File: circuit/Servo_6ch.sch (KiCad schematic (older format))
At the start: 24 parts, among them IC1 TLP521, IC2 TLP521, IC3 TLP521, IC4 TLP521, IC5 TLP521, IC6 TLP521, J3 servo0, J4 servo1, J5 servo2, J6 servo0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

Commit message: 回路図と部品表完了
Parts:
- J3, J4, J5, J6, J7, J8: footprint (none) -> YASU:XA_3Pin
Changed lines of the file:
@@
 F 0 "J3" H 5400 2650 50  0000 C CNN
 F 1 "servo0" V 5500 2450 50  0000 C CNN
-F 2 "" H 5400 2450 50  0001 C CNN
+F 2 "YASU:XA_3Pin" H 5400 2450 50  0001 C CNN
 F 3 "" H 5400 2450 50  0001 C CNN
 	1    5400 2450
@@
 F 0 "J5" H 5400 5050 50  0000 C CNN
 F 1 "servo2" V 5500 4850 50  0000 C CNN
-F 2 "" H 5400 4850 50  0001 C CNN
+F 2 "YASU:XA_3Pin" H 5400 4850 50  0001 C CNN
 F 3 "" H 5400 4850 50  0001 C CNN
 	1    5400 4850
@@
 F 0 "J4" H 5400 3800 50  0000 C CNN
 F 1 "servo1" V 5500 3600 50  0000 C CNN
-F 2 "" H 5400 3600 50  0001 C CNN
+F 2 "YASU:XA_3Pin" H 5400 3600 50  0001 C CNN
 F 3 "" H 5400 3600 50  0001 C CNN
 	1    5400 3600
@@
 F 0 "J6" H 8300 2650 50  0000 C CNN
 F 1 "servo0" V 8400 2450 50  0000 C CNN
-F 2 "" H 8300 2450 50  0001 C CNN
+F 2 "YASU:XA_3Pin" H 8300 2450 50  0001 C CNN
 F 3 "" H 8300 2450 50  0001 C CNN
 	1    8300 2450
@@
 F 0 "J8" H 8300 5050 50  0000 C CNN
 F 1 "servo2" V 8400 4850 50  0000 C CNN
-F 2 "" H 8300 4850 50  0001 C CNN
+F 2 "YASU:XA_3Pin" H 8300 4850 50  0001 C CNN
 F 3 "" H 8300 4850 50  0001 C CNN
 	1    8300 4850
@@
 F 0 "J7" H 8300 3800 50  0000 C CNN
 F 1 "servo1" V 8400 3600 50  0000 C CNN
-F 2 "" H 8300 3600 50  0001 C CNN
+F 2 "YASU:XA_3Pin" H 8300 3600 50  0001 C CNN
 F 3 "" H 8300 3600 50  0001 C CNN
 	1    8300 3600

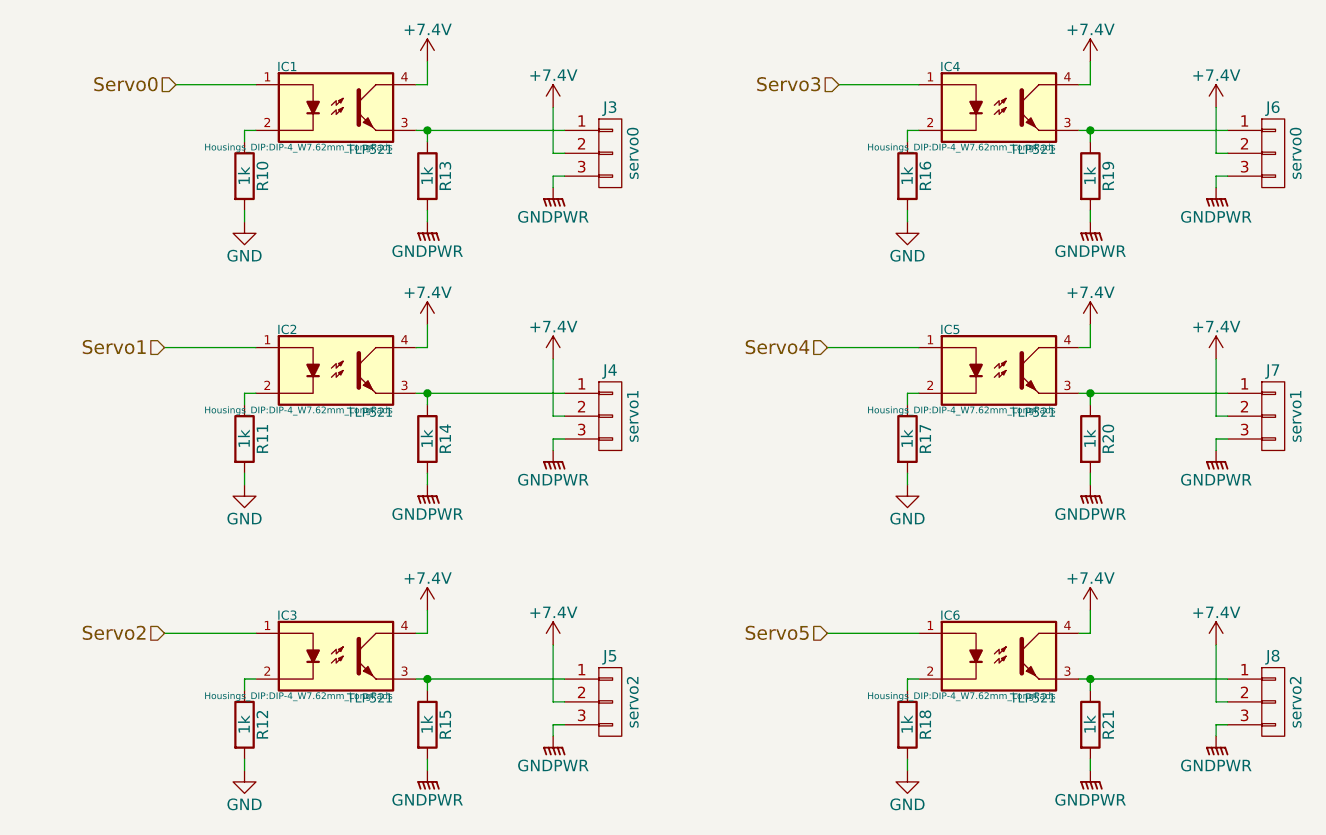
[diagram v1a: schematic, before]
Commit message: 実態配線図の部品配置を大まかに決定
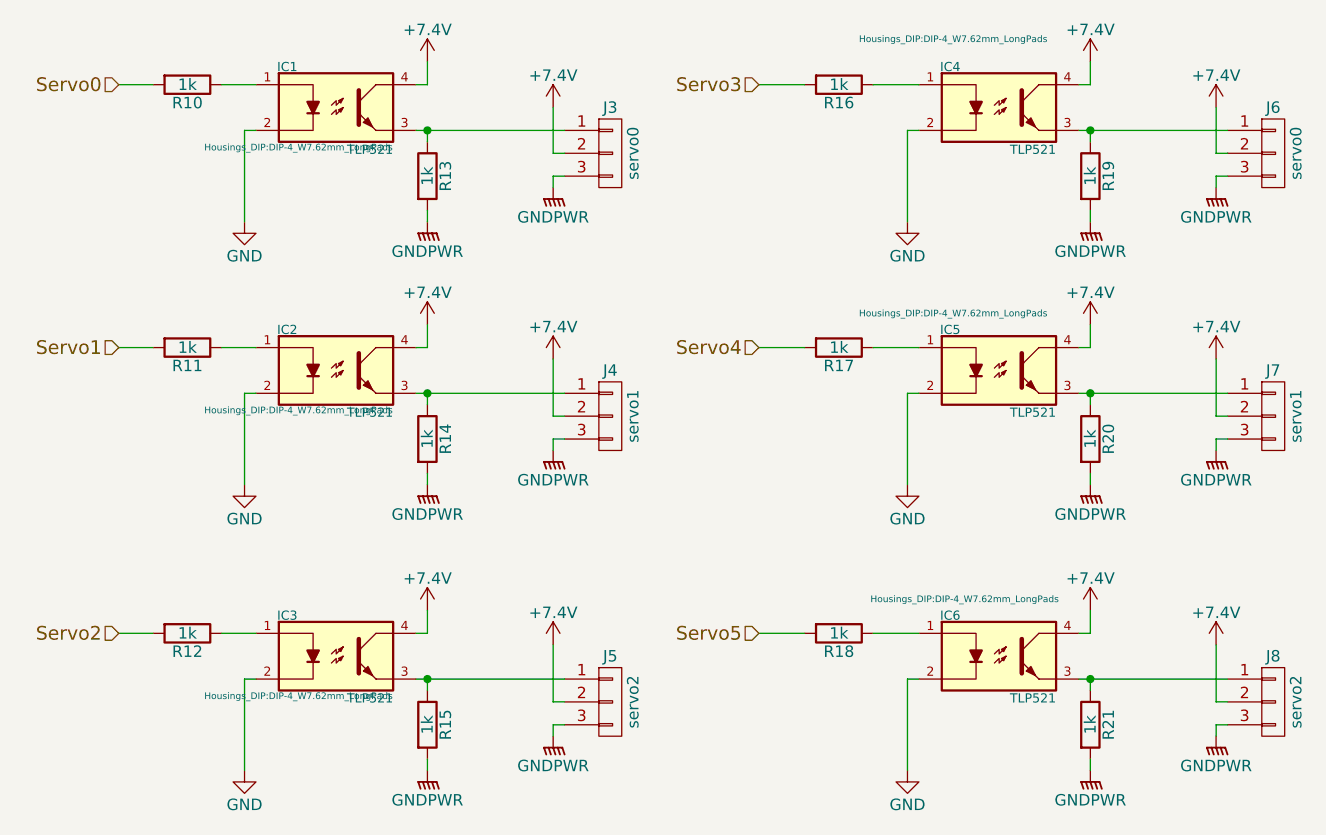
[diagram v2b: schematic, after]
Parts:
- J3, J4, J5, J6, J7, J8: footprint YASU:XA_3Pin -> YASU:XA_3Pin_LP
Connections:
- net GND: now also IC1.2, IC2.2, IC3.2, IC4.2, IC5.2, IC6.2; no longer R10.2, R11.2, R12.2, R16.2, R17.2, R18.2
- net Servo0: now also R10.2; no longer IC1.1
- net Servo1: now also R11.2; no longer IC2.1
- net Servo2: now also R12.2; no longer IC3.1
- net Servo3: now also R16.2; no longer IC4.1
- net Servo4: now also R17.2; no longer IC5.1
- net Servo5: now also R18.2; no longer IC6.1
- net at R10.1: now also IC1.1; no longer IC1.2
- net at R11.1: now also IC2.1; no longer IC2.2
- net at R12.1: now also IC3.1; no longer IC3.2
- net at R16.1: now also IC4.1; no longer IC4.2
- net at R17.1: now also IC5.1; no longer IC5.2
- net at R18.1: now also IC6.1; no longer IC6.2
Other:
- moved on the sheet: R10, R11, R12, R16, R17, R18
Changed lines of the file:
@@
 LIBS:valves
 LIBS:stm32
-LIBS:robocon_sch
-LIBS:SamacSys_Parts
-LIBS:YASU
 LIBS:ServoDriver-cache
 EELAYER 25 0
@@
 F 0 "J3" H 5400 2650 50  0000 C CNN
 F 1 "servo0" V 5500 2450 50  0000 C CNN
-F 2 "YASU:XA_3Pin" H 5400 2450 50  0001 C CNN
+F 2 "YASU:XA_3Pin_LP" H 5400 2450 50  0001 C CNN
 F 3 "" H 5400 2450 50  0001 C CNN
 	1    5400 2450
@@
 F 0 "J5" H 5400 5050 50  0000 C CNN
 F 1 "servo2" V 5500 4850 50  0000 C CNN
-F 2 "YASU:XA_3Pin" H 5400 4850 50  0001 C CNN
+F 2 "YASU:XA_3Pin_LP" H 5400 4850 50  0001 C CNN
 F 3 "" H 5400 4850 50  0001 C CNN
 	1    5400 4850
@@
 F 0 "J4" H 5400 3800 50  0000 C CNN
 F 1 "servo1" V 5500 3600 50  0000 C CNN
-F 2 "YASU:XA_3Pin" H 5400 3600 50  0001 C CNN
+F 2 "YASU:XA_3Pin_LP" H 5400 3600 50  0001 C CNN
 F 3 "" H 5400 3600 50  0001 C CNN
 	1    5400 3600
@@
 $EndComp
 Wire Wire Line
-	3500 2150 3850 2150
-Wire Wire Line
 	5200 2450 5150 2450
 Wire Wire Line
@@
 L R R11
 U 1 1 5955C6E2
-P 3800 3700
-F 0 "R11" V 3880 3700 50  0000 C CNN
-F 1 "1k" V 3800 3700 50  0000 C CNN
-F 2 "Resistors_SMD:R_0603_HandSoldering" V 3730 3700 50  0001 C CNN
-F 3 "" H 3800 3700 50  0001 C CNN
-	1    3800 3700
-	1    0    0    -1
-$EndComp
-Wire Wire Line
-	3800 3550 3800 3500
+P 3550 3300
+F 0 "R11" V 3630 3300 50  0000 C CNN
+F 1 "1k" V 3550 3300 50  0000 C CNN
+F 2 "Resistors_SMD:R_0603_HandSoldering" V 3480 3300 50  0001 C CNN
+F 3 "" H 3550 3300 50  0001 C CNN
+	1    3550 3300
+	0    1    1    0
+$EndComp
+Wire Wire Line
+	3800 3500 3800 3900
 Wire Wire Line
 	3800 3500 3850 3500
-Wire Wire Line
-	3850 3300 3450 3300
-Wire Wire Line
-	3800 3850 3800 3900
 Wire Wire Line
 	4600 3900 4600 3850
@@
 L R R10
 U 1 1 5955C6EF
-P 3800 2550
-F 0 "R10" V 3880 2550 50  0000 C CNN
-F 1 "1k" V 3800 2550 50  0000 C CNN
-F 2 "Resistors_SMD:R_0603_HandSoldering" V 3730 2550 50  0001 C CNN
-F 3 "" H 3800 2550 50  0001 C CNN
-	1    3800 2550
-	1    0    0    -1
-$EndComp
-Wire Wire Line
-	3800 2400 3800 2350
+P 3550 2150
+F 0 "R10" V 3630 2150 50  0000 C CNN
+F 1 "1k" V 3550 2150 50  0000 C CNN
+F 2 "Resistors_SMD:R_0603_HandSoldering" V 3480 2150 50  0001 C CNN
+F 3 "" H 3550 2150 50  0001 C CNN
+	1    3550 2150
+	0    1    1    0
+$EndComp
+Wire Wire Line
+	3800 2350 3800 2750
 Wire Wire Line
 	3800 2350 3850 2350
-Wire Wire Line
-	3800 2700 3800 2750
 $Comp
 L GND #PWR042
@@
 L R R12
 U 1 1 5955C757
-P 3800 4950
-F 0 "R12" V 3880 4950 50  0000 C CNN
-F 1 "1k" V 3800 4950 50  0000 C CNN
-F 2 "Resistors_SMD:R_0603_HandSoldering" V 3730 4950 50  0001 C CNN
-F 3 "" H 3800 4950 50  0001 C CNN
-	1    3800 4950
-	1    0    0    -1
-$EndComp
-Wire Wire Line
-	3800 4800 3800 4750
+P 3550 4550
+F 0 "R12" V 3630 4550 50  0000 C CNN
+F 1 "1k" V 3550 4550 50  0000 C CNN
+F 2 "Resistors_SMD:R_0603_HandSoldering" V 3480 4550 50  0001 C CNN
+F 3 "" H 3550 4550 50  0001 C CNN
+	1    3550 4550
+	0    1    1    0
+$EndComp
+Wire Wire Line
+	3800 4750 3800 5150
 Wire Wire Line
 	3800 4750 3850 4750
-Wire Wire Line
-	3850 4550 3450 4550
-Wire Wire Line
-	3800 5100 3800 5150
 Wire Wire Line
 	4600 5150 4600 5100
@@
 	1    0    0    -1
 $EndComp
-Text HLabel 3500 2150 0    60   Input ~ 0
+Text HLabel 3250 2150 0    60   Input ~ 0
 Servo0
-Text HLabel 3450 3300 0    60   Input ~ 0
+Text HLabel 3250 3300 0    60   Input ~ 0
 Servo1
-Text HLabel 3450 4550 0    60   Input ~ 0
+Text HLabel 3250 4550 0    60   Input ~ 0
 Servo2
 $Comp
@@
 F 0 "J6" H 8300 2650 50  0000 C CNN
 F 1 "servo0" V 8400 2450 50  0000 C CNN
-F 2 "YASU:XA_3Pin" H 8300 2450 50  0001 C CNN
+F 2 "YASU:XA_3Pin_LP" H 8300 2450 50  0001 C CNN
 F 3 "" H 8300 2450 50  0001 C CNN
 	1    8300 2450
@@
 F 0 "J8" H 8300 5050 50  0000 C CNN
 F 1 "servo2" V 8400 4850 50  0000 C CNN
-F 2 "YASU:XA_3Pin" H 8300 4850 50  0001 C CNN
+F 2 "YASU:XA_3Pin_LP" H 8300 4850 50  0001 C CNN
 F 3 "" H 8300 4850 50  0001 C CNN
 	1    8300 4850
@@
 F 0 "J7" H 8300 3800 50  0000 C CNN
 F 1 "servo1" V 8400 3600 50  0000 C CNN
-F 2 "YASU:XA_3Pin" H 8300 3600 50  0001 C CNN
+F 2 "YASU:XA_3Pin_LP" H 8300 3600 50  0001 C CNN
 F 3 "" H 8300 3600 50  0001 C CNN
 	1    8300 3600
@@
 $EndComp
 Wire Wire Line
-	6400 2150 6750 2150
-Wire Wire Line
 	8100 2450 8050 2450
 Wire Wire Line
@@
 F 0 "IC4" H 6887 2428 40  0000 C CNN
 F 1 "TLP521" H 7249 2066 40  0000 C CNN
-F 2 "Housings_DIP:DIP-4_W7.62mm_LongPads" H 6936 2076 29  0000 C CNN
+F 2 "Housings_DIP:DIP-4_W7.62mm_LongPads" H 6900 2550 29  0000 C CNN
 F 3 "" H 7100 2250 60  0000 C CNN
 	1    7100 2250
@@
 F 0 "IC5" H 6887 3578 40  0000 C CNN
 F 1 "TLP521" H 7249 3216 40  0000 C CNN
-F 2 "Housings_DIP:DIP-4_W7.62mm_LongPads" H 6936 3226 29  0000 C CNN
+F 2 "Housings_DIP:DIP-4_W7.62mm_LongPads" H 6900 3650 29  0000 C CNN
 F 3 "" H 7100 3400 60  0000 C CNN
 	1    7100 3400
@@
 L R R17
 U 1 1 5971CE90
-P 6700 3700
-F 0 "R17" V 6780 3700 50  0000 C CNN
-F 1 "1k" V 6700 3700 50  0000 C CNN
-F 2 "Resistors_SMD:R_0603_HandSoldering" V 6630 3700 50  0001 C CNN
-F 3 "" H 6700 3700 50  0001 C CNN
-	1    6700 3700
-	1    0    0    -1
-$EndComp
-Wire Wire Line
-	6700 3550 6700 3500
+P 6400 3300
+F 0 "R17" V 6480 3300 50  0000 C CNN
+F 1 "1k" V 6400 3300 50  0000 C CNN
+F 2 "Resistors_SMD:R_0603_HandSoldering" V 6330 3300 50  0001 C CNN
+F 3 "" H 6400 3300 50  0001 C CNN
+	1    6400 3300
+	0    1    1    0
+$EndComp
+Wire Wire Line
+	6700 3500 6700 3900
 Wire Wire Line
 	6700 3500 6750 3500
-Wire Wire Line
-	6750 3300 6350 3300
-Wire Wire Line
-	6700 3850 6700 3900
 Wire Wire Line
 	7500 3900 7500 3850
@@
 L R R16
 U 1 1 5971CE9C
-P 6700 2550
-F 0 "R16" V 6780 2550 50  0000 C CNN
-F 1 "1k" V 6700 2550 50  0000 C CNN
-F 2 "Resistors_SMD:R_0603_HandSoldering" V 6630 2550 50  0001 C CNN
-F 3 "" H 6700 2550 50  0001 C CNN
-	1    6700 2550
-	1    0    0    -1
-$EndComp
-Wire Wire Line
-	6700 2400 6700 2350
+P 6400 2150
+F 0 "R16" V 6480 2150 50  0000 C CNN
+F 1 "1k" V 6400 2150 50  0000 C CNN
+F 2 "Resistors_SMD:R_0603_HandSoldering" V 6330 2150 50  0001 C CNN
+F 3 "" H 6400 2150 50  0001 C CNN
+	1    6400 2150
+	0    1    1    0
+$EndComp
+Wire Wire Line
+	6700 2350 6700 2750
 Wire Wire Line
 	6700 2350 6750 2350
-Wire Wire Line
-	6700 2700 6700 2750
 $Comp
 L GND #PWR057
@@
 F 0 "IC6" H 6887 4828 40  0000 C CNN
 F 1 "TLP521" H 7249 4466 40  0000 C CNN
-F 2 "Housings_DIP:DIP-4_W7.62mm_LongPads" H 6936 4476 29  0000 C CNN
+F 2 "Housings_DIP:DIP-4_W7.62mm_LongPads" H 6950 4900 29  0000 C CNN
 F 3 "" H 7100 4650 60  0000 C CNN
 	1    7100 4650
@@
 L R R18
 U 1 1 5971CECE
-P 6700 4950
-F 0 "R18" V 6780 4950 50  0000 C CNN
-F 1 "1k" V 6700 4950 50  0000 C CNN
-F 2 "Resistors_SMD:R_0603_HandSoldering" V 6630 4950 50  0001 C CNN
-F 3 "" H 6700 4950 50  0001 C CNN
-	1    6700 4950
-	1    0    0    -1
-$EndComp
-Wire Wire Line
-	6700 4800 6700 4750
+P 6400 4550
+F 0 "R18" V 6480 4550 50  0000 C CNN
+F 1 "1k" V 6400 4550 50  0000 C CNN
+F 2 "Resistors_SMD:R_0603_HandSoldering" V 6330 4550 50  0001 C CNN
+F 3 "" H 6400 4550 50  0001 C CNN
+	1    6400 4550
+	0    1    1    0
+$EndComp
+Wire Wire Line
+	6700 4750 6700 5150
 Wire Wire Line
 	6700 4750 6750 4750
-Wire Wire Line
-	6750 4550 6350 4550
-Wire Wire Line
-	6700 5100 6700 5150
 Wire Wire Line
 	7500 5150 7500 5100
@@
 	1    0    0    -1
 $EndComp
-Text HLabel 6400 2150 0    60   Input ~ 0
+Text HLabel 6050 2150 0    60   Input ~ 0
 Servo3
-Text HLabel 6350 3300 0    60   Input ~ 0
+Text HLabel 6050 3300 0    60   Input ~ 0
 Servo4
-Text HLabel 6350 4550 0    60   Input ~ 0
+Text HLabel 6050 4550 0    60   Input ~ 0
 Servo5
+Wire Wire Line
+	3250 3300 3400 3300
+Wire Wire Line
+	3700 3300 3850 3300
+Wire Wire Line
+	3850 4550 3700 4550
+Wire Wire Line
+	3400 4550 3250 4550
+Wire Wire Line
+	3250 2150 3400 2150
+Wire Wire Line
+	3700 2150 3850 2150
+Wire Wire Line
+	6050 2150 6250 2150
+Wire Wire Line
+	6550 2150 6750 2150
+Wire Wire Line
+	6050 3300 6250 3300
+Wire Wire Line
+	6550 3300 6750 3300
+Wire Wire Line
+	6050 4550 6250 4550
+Wire Wire Line
+	6550 4550 6750 4550
 $EndSCHEMATC

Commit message: 抵抗の大きさを変更
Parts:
- R13, R14, R15, R19, R20, R21: footprint Resistors_SMD:R_0603_HandSoldering -> Resistors_THT:R_Axial_DIN0207_L6.3mm_D2.5mm_P7.62mm_Horizontal
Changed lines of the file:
@@
 F 0 "R13" V 4680 2550 50  0000 C CNN
 F 1 "1k" V 4600 2550 50  0000 C CNN
-F 2 "Resistors_SMD:R_0603_HandSoldering" V 4530 2550 50  0001 C CNN
+F 2 "Resistors_THT:R_Axial_DIN0207_L6.3mm_D2.5mm_P7.62mm_Horizontal" V 4530 2550 50  0001 C CNN
 F 3 "" H 4600 2550 50  0001 C CNN
 	1    4600 2550
@@
 F 0 "R14" V 4680 3700 50  0000 C CNN
 F 1 "1k" V 4600 3700 50  0000 C CNN
-F 2 "Resistors_SMD:R_0603_HandSoldering" V 4530 3700 50  0001 C CNN
+F 2 "Resistors_THT:R_Axial_DIN0207_L6.3mm_D2.5mm_P7.62mm_Horizontal" V 4530 3700 50  0001 C CNN
 F 3 "" H 4600 3700 50  0001 C CNN
 	1    4600 3700
@@
 F 0 "R15" V 4680 4950 50  0000 C CNN
 F 1 "1k" V 4600 4950 50  0000 C CNN
-F 2 "Resistors_SMD:R_0603_HandSoldering" V 4530 4950 50  0001 C CNN
+F 2 "Resistors_THT:R_Axial_DIN0207_L6.3mm_D2.5mm_P7.62mm_Horizontal" V 4530 4950 50  0001 C CNN
 F 3 "" H 4600 4950 50  0001 C CNN
 	1    4600 4950
@@
 F 0 "R19" V 7580 2550 50  0000 C CNN
 F 1 "1k" V 7500 2550 50  0000 C CNN
-F 2 "Resistors_SMD:R_0603_HandSoldering" V 7430 2550 50  0001 C CNN
+F 2 "Resistors_THT:R_Axial_DIN0207_L6.3mm_D2.5mm_P7.62mm_Horizontal" V 7430 2550 50  0001 C CNN
 F 3 "" H 7500 2550 50  0001 C CNN
 	1    7500 2550
@@
 F 0 "R20" V 7580 3700 50  0000 C CNN
 F 1 "1k" V 7500 3700 50  0000 C CNN
-F 2 "Resistors_SMD:R_0603_HandSoldering" V 7430 3700 50  0001 C CNN
+F 2 "Resistors_THT:R_Axial_DIN0207_L6.3mm_D2.5mm_P7.62mm_Horizontal" V 7430 3700 50  0001 C CNN
 F 3 "" H 7500 3700 50  0001 C CNN
 	1    7500 3700
@@
 F 0 "R21" V 7580 4950 50  0000 C CNN
 F 1 "1k" V 7500 4950 50  0000 C CNN
-F 2 "Resistors_SMD:R_0603_HandSoldering" V 7430 4950 50  0001 C CNN
+F 2 "Resistors_THT:R_Axial_DIN0207_L6.3mm_D2.5mm_P7.62mm_Horizontal" V 7430 4950 50  0001 C CNN
 F 3 "" H 7500 4950 50  0001 C CNN
 	1    7500 4950

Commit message: チップ抵抗の大きさ変更とガーバー出力のための手直し
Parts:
- R10, R11, R12, R16, R17, R18: footprint Resistors_SMD:R_0603_HandSoldering -> YASU:R_0603_HandSoldering_LP
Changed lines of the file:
@@
 F 0 "R11" V 3630 3300 50  0000 C CNN
 F 1 "1k" V 3550 3300 50  0000 C CNN
-F 2 "Resistors_SMD:R_0603_HandSoldering" V 3480 3300 50  0001 C CNN
+F 2 "YASU:R_0603_HandSoldering_LP" V 3480 3300 50  0001 C CNN
 F 3 "" H 3550 3300 50  0001 C CNN
 	1    3550 3300
@@
 F 0 "R10" V 3630 2150 50  0000 C CNN
 F 1 "1k" V 3550 2150 50  0000 C CNN
-F 2 "Resistors_SMD:R_0603_HandSoldering" V 3480 2150 50  0001 C CNN
+F 2 "YASU:R_0603_HandSoldering_LP" V 3480 2150 50  0001 C CNN
 F 3 "" H 3550 2150 50  0001 C CNN
 	1    3550 2150
@@
 F 0 "R12" V 3630 4550 50  0000 C CNN
 F 1 "1k" V 3550 4550 50  0000 C CNN
-F 2 "Resistors_SMD:R_0603_HandSoldering" V 3480 4550 50  0001 C CNN
+F 2 "YASU:R_0603_HandSoldering_LP" V 3480 4550 50  0001 C CNN
 F 3 "" H 3550 4550 50  0001 C CNN
 	1    3550 4550
@@
 F 0 "R17" V 6480 3300 50  0000 C CNN
 F 1 "1k" V 6400 3300 50  0000 C CNN
-F 2 "Resistors_SMD:R_0603_HandSoldering" V 6330 3300 50  0001 C CNN
+F 2 "YASU:R_0603_HandSoldering_LP" V 6330 3300 50  0001 C CNN
 F 3 "" H 6400 3300 50  0001 C CNN
 	1    6400 3300
@@
 F 0 "R16" V 6480 2150 50  0000 C CNN
 F 1 "1k" V 6400 2150 50  0000 C CNN
-F 2 "Resistors_SMD:R_0603_HandSoldering" V 6330 2150 50  0001 C CNN
+F 2 "YASU:R_0603_HandSoldering_LP" V 6330 2150 50  0001 C CNN
 F 3 "" H 6400 2150 50  0001 C CNN
 	1    6400 2150
@@
 F 0 "R18" V 6480 4550 50  0000 C CNN
 F 1 "1k" V 6400 4550 50  0000 C CNN
-F 2 "Resistors_SMD:R_0603_HandSoldering" V 6330 4550 50  0001 C CNN
+F 2 "YASU:R_0603_HandSoldering_LP" V 6330 4550 50  0001 C CNN
 F 3 "" H 6400 4550 50  0001 C CNN
 	1    6400 4550
